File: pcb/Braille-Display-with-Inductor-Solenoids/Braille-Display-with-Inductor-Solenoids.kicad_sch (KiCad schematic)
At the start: 23 parts, among them J1 Screw_Terminal_01x02, J2 Screw_Terminal_01x02, J3 Screw_Terminal_01x02, J4 Conn_01x03, J5 Conn_01x02, J6 Conn_01x08, SW1 SW_Push, SW2 SW_Push, U1 RP2040-Zero

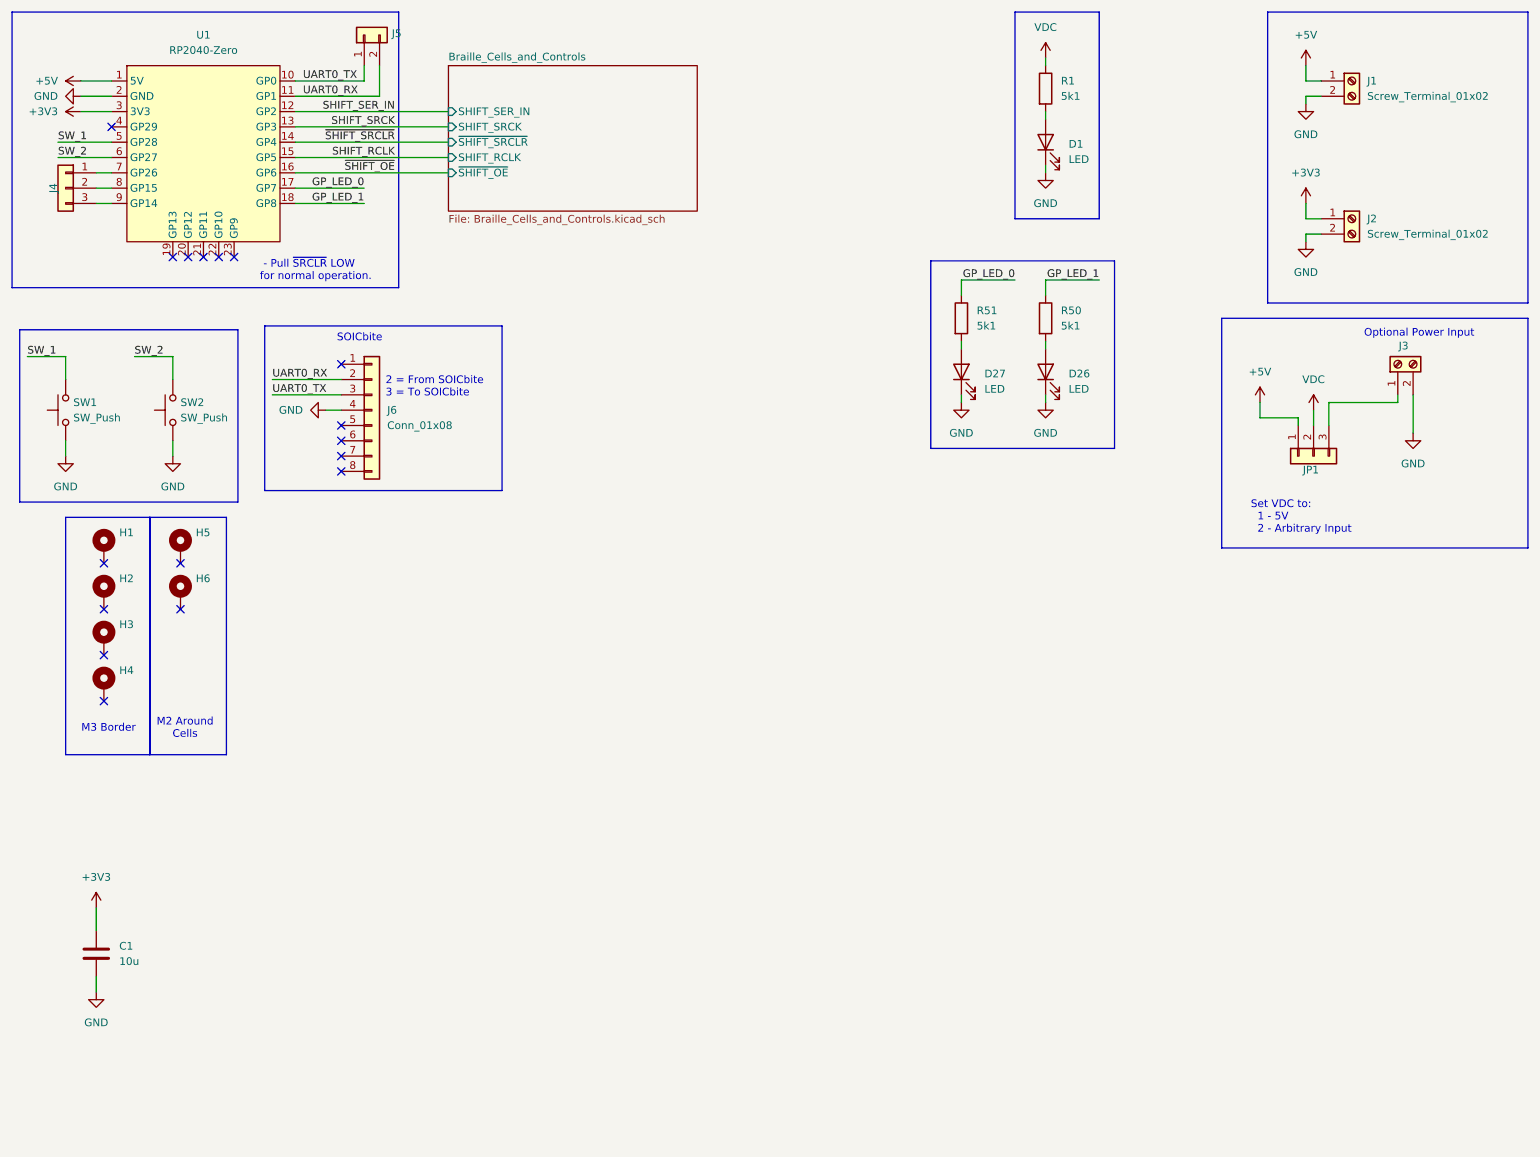
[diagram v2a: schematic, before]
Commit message: pcb: WIP - Switch to new parts, layout
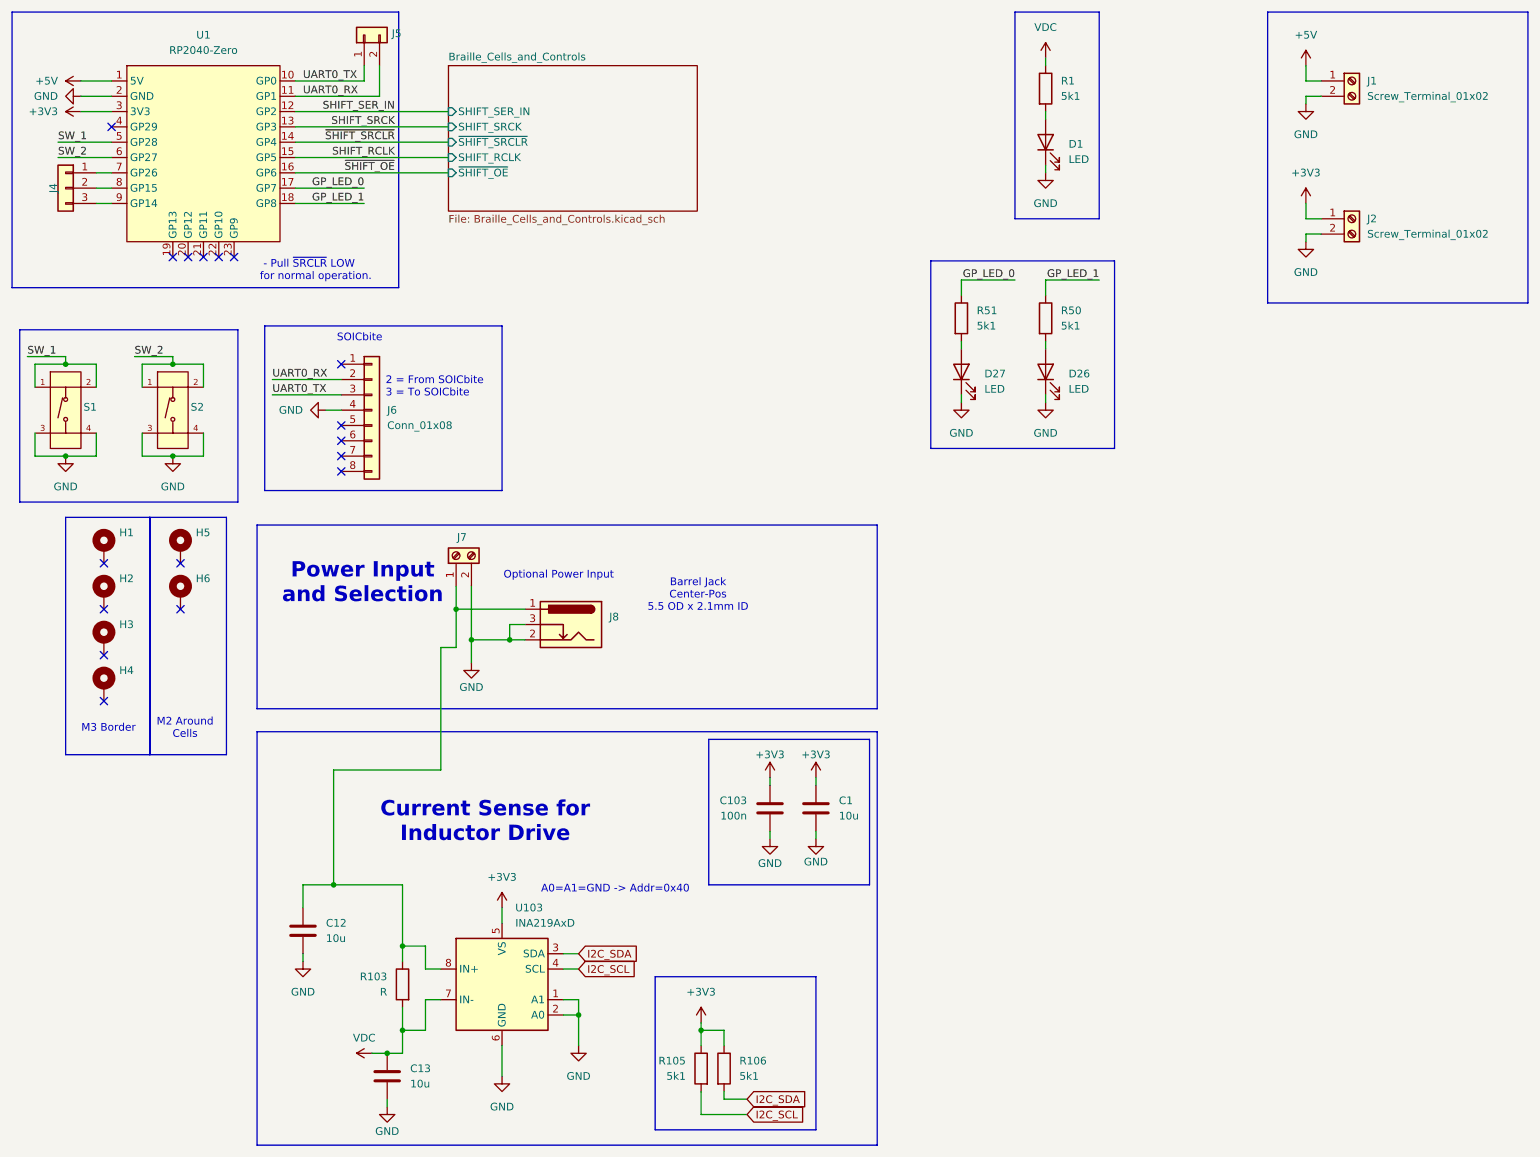
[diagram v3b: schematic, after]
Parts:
- removed J3: Screw_Terminal_01x02, TerminalBlock:TerminalBlock_bornier-2_P5.08mm, symbol Connector:Screw_Terminal_01x02
- removed JP1: SolderJumper_3_Open, Connector_PinHeader_2.54mm:PinHeader_1x03_P2.54mm_Vertical, symbol Connector_Generic:Conn_01x03
- removed SW1, SW2: SW_Push, 00-project-footprints:PushButtonSMD_2.93x3.9, symbol Switch:SW_Push
- added C103: 100n, Capacitor_SMD:C_0603_1608Metric_Pad1.08x0.95mm_HandSolder, symbol Device:C
- added C12, C13: 10u, Capacitor_SMD:C_1206_3216Metric_Pad1.33x1.80mm_HandSolder, symbol Device:C
- added J7: Screw_Terminal_01x02, TerminalBlock:TerminalBlock_bornier-2_P5.08mm, symbol Connector:Screw_Terminal_01x02
- added J8: Barrel_Jack_Switch, Connector_BarrelJack:BarrelJack_Horizontal, symbol Connector:Barrel_Jack_Switch
- added R103: R, Resistor_SMD:R_1206_3216Metric_Pad1.30x1.75mm_HandSolder, symbol Device:R
- added R105, R106: 5k1, Resistor_SMD:R_0603_1608Metric_Pad0.98x0.95mm_HandSolder, symbol Device:R
- added S1, S2: Tactile Button, 160gf, PCM_JLCPCB:SW-SMD_4P-L5.1-W5.1-P3.70-LS6.5-TL-2, symbol PCM_JLCPCB-Connectors_Buttons:Tactile Button, 160gf
- added U103: INA219AxD, Package_SO:SOIC-8_3.9x4.9mm_P1.27mm, symbol Sensor_Energy:INA219AxD
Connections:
- net +3V3: now also C103.1, R105.1, R106.1, U103.5 (VS)
- net GND: now also C103.2, C12.2, C13.2, J7.2 (Pin_2), J8.2, J8.3, S1.3 (C), S1.4 (D), S2.3 (C), S2.4 (D), U103.1 (A1), U103.2 (A0), U103.6 (GND)
- net SW_1: now also S1.1 (A), S1.2 (B)
- net SW_2: now also S2.1 (A), S2.2 (B)
- net VDC: now also C13.1, R103.2, U103.7 (IN-)
- new net: C12.1, J7.1 (Pin_1), J8.1, R103.1, U103.8 (IN+)
- new net I2C_SCL: R105.2, U103.4 (SCL)
- new net I2C_SDA: R106.2, U103.3 (SDA)
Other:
- note added: "A0=A1=GND -> Addr=0x40"
- note added: "Barrel Jack Center-Pos 5.5 OD x 2.1mm ID"
- note added: "Current Sense for Inductor Drive"
- note added: "Power Input and Selection"
- note removed: "Set VDC to: 1 - 5V 2 - Arbitrary Input"
- moved on the sheet: C1

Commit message: pcb: WIP - High power and repeated routing
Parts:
- removed J4: Conn_01x03, Connector_PinHeader_2.54mm:PinHeader_1x03_P2.54mm_Vertical, symbol Connector_Generic:Conn_01x03
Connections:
- net I2C_SCL: now also U1.8 (GP15)
- net I2C_SDA: now also U1.9 (GP14)
- no-connect marks 17 -> 18
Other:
- note added: "I2C Port #1"
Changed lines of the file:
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@@
 		)
 	)
+	(text "I2C Port #1"
+		(exclude_from_sim no)
+		(at 24.13 49.784 0)
+		(effects
+			(font
+				(size 1.27 1.27)
+				(thickness 0.254)
+				(bold yes)
+			)
+		)
+	)
 	(text "SOICbite"
 		(exclude_from_sim no)
@@
 	)
 	(no_connect
+		(at 30.48 40.64)
+	)
+	(no_connect
 		(at 48.26 54.61)
 	)
@@
 	(wire
 		(pts
+			(xy 26.67 45.72) (xy 30.48 45.72)
+		)
+		(stroke
+			(width 0)
+			(type default)
+		)
+	)
+	(wire
+		(pts
 			(xy 17.78 76.2) (xy 17.78 72.39)
 		)
@@
 	(wire
 		(pts
+			(xy 26.67 43.18) (xy 30.48 43.18)
+		)
+		(stroke
+			(width 0)
+			(type default)
+		)
+	)
+	(wire
+		(pts
 			(xy 228.6 22.86) (xy 228.6 25.4)
 		)
@@
 	(wire
 		(pts
-			(xy 27.94 45.72) (xy 30.48 45.72)
-		)
-		(stroke
-			(width 0)
-			(type default)
-		)
-	)
-	(wire
-		(pts
 			(xy 228.6 52.07) (xy 228.6 50.8)
 		)
@@
 	(wire
 		(pts
-			(xy 27.94 43.18) (xy 30.48 43.18)
-		)
-		(stroke
-			(width 0)
-			(type default)
-		)
-	)
-	(wire
-		(pts
 			(xy 60.96 33.02) (xy 86.36 33.02)
 		)
@@
 	(wire
 		(pts
-			(xy 27.94 40.64) (xy 30.48 40.64)
-		)
-		(stroke
-			(width 0)
-			(type default)
-		)
-	)
-	(wire
-		(pts
 			(xy 78.74 182.88) (xy 78.74 179.07)
 		)
@@
 		)
 	)
+	(global_label "I2C_SDA"
+		(shape input)
+		(at 26.67 45.72 180)
+		(fields_autoplaced yes)
+		(effects
+			(font
+				(size 1.27 1.27)
+			)
+			(justify right)
+		)
+		(property "Intersheetrefs" "${INTERSHEET_REFS}"
+			(at 16.1253 45.72 0)
+			(effects
+				(font
+					(size 1.27 1.27)
+				)
+				(justify right)
+				(hide yes)
+			)
+		)
+	)
 	(global_label "I2C_SCL"
 		(shape input)
@@
 	(global_label "I2C_SCL"
 		(shape input)
+		(at 26.67 43.18 180)
+		(fields_autoplaced yes)
+		(effects
+			(font
+				(size 1.27 1.27)
+			)
+			(justify right)
+		)
+		(property "Intersheetrefs" "${INTERSHEET_REFS}"
+			(at 16.0648 43.18 0)
+			(effects
+				(font
+					(size 1.27 1.27)
+				)
+				(justify right)
+				(hide yes)
+			)
+		)
+	)
+	(global_label "I2C_SCL"
+		(shape input)
 		(at 135.89 196.85 0)
 		(fields_autoplaced yes)
@@
 					(unit 1)
 				)
-			)
-		)
-	)
-	(symbol
-		(lib_id "Connector_Generic:Conn_01x03")
-		(at 22.86 43.18 0)
-		(mirror y)
-		(unit 1)
-		(exclude_from_sim no)
-		(in_bom yes)
-		(on_board yes)
-		(dnp no)
-		(property "Reference" "J4"
-			(at 20.828 43.18 90)
-			(effects
-				(font
-					(size 1.27 1.27)
-				)
-			)
-		)
-		(property "Value" "Conn_01x03"
-			(at 22.86 36.83 0)
-			(effects
-				(font
-					(size 1.27 1.27)
-				)
-				(hide yes)
-			)
-		)
-		(property "Footprint" "Connector_PinHeader_2.54mm:PinHeader_1x03_P2.54mm_Vertical"
-			(at 22.86 43.18 0)
-			(effects
-				(font
-					(size 1.27 1.27)
-				)
-				(hide yes)
-			)
-		)
-		(property "Datasheet" "~"
-			(at 22.86 43.18 0)
-			(effects
-				(font
-					(size 1.27 1.27)
-				)
-				(hide yes)
-			)
-		)
-		(property "Description" "Generic connector, single row, 01x03, script generated (kicad-library-utils/schlib/autogen/connector/)"
-			(at 22.86 43.18 0)
-			(effects
-				(font
-					(size 1.27 1.27)
-				)
-				(hide yes)
-			)
-		)
-		(pin "3"
-		)
-		(pin "2"
-		)
-		(pin "1"
-		)
-		(instances
-			(project ""
-				(path "/3829a125-89bd-48f9-bfbe-92d753eb8f7f"
-					(reference "J4")
-					(unit 1)
-				)
